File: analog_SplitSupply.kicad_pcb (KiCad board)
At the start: 2 copper layers, 50.8 x 50.8 mm, 51 parts, among them J1 Conn_01x04, J2 Conn_01x02, J3 Conn_01x02, J4 Conn_01x02, J5 Conn_01x02, J6 Conn_01x04, U1 TI_LM2734ZMK_NOPB, U2 AD_LT1054CS8#TRPBF, U3 TI_TLV1117CDCY, U4 AD_LT1175CS8#PBF

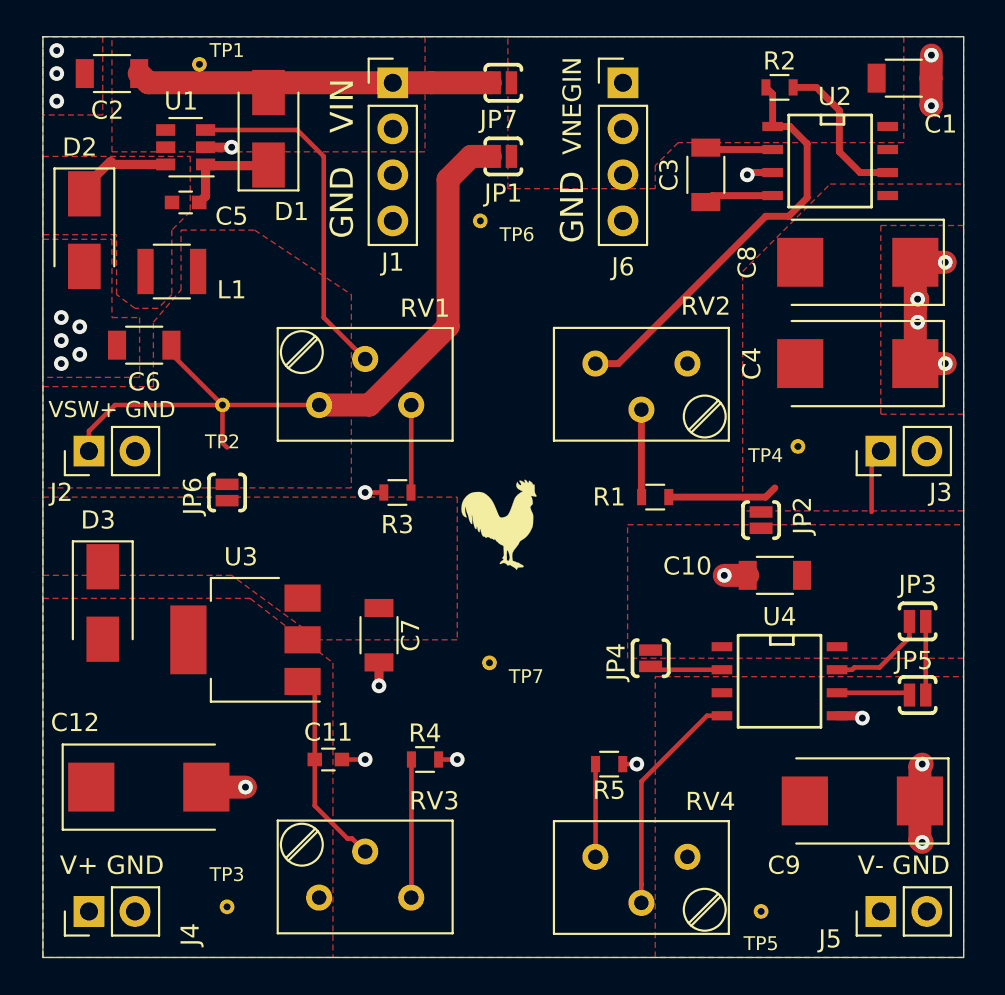
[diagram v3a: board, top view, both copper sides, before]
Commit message: Added logos, updated jumpers, and added second set of output headers.
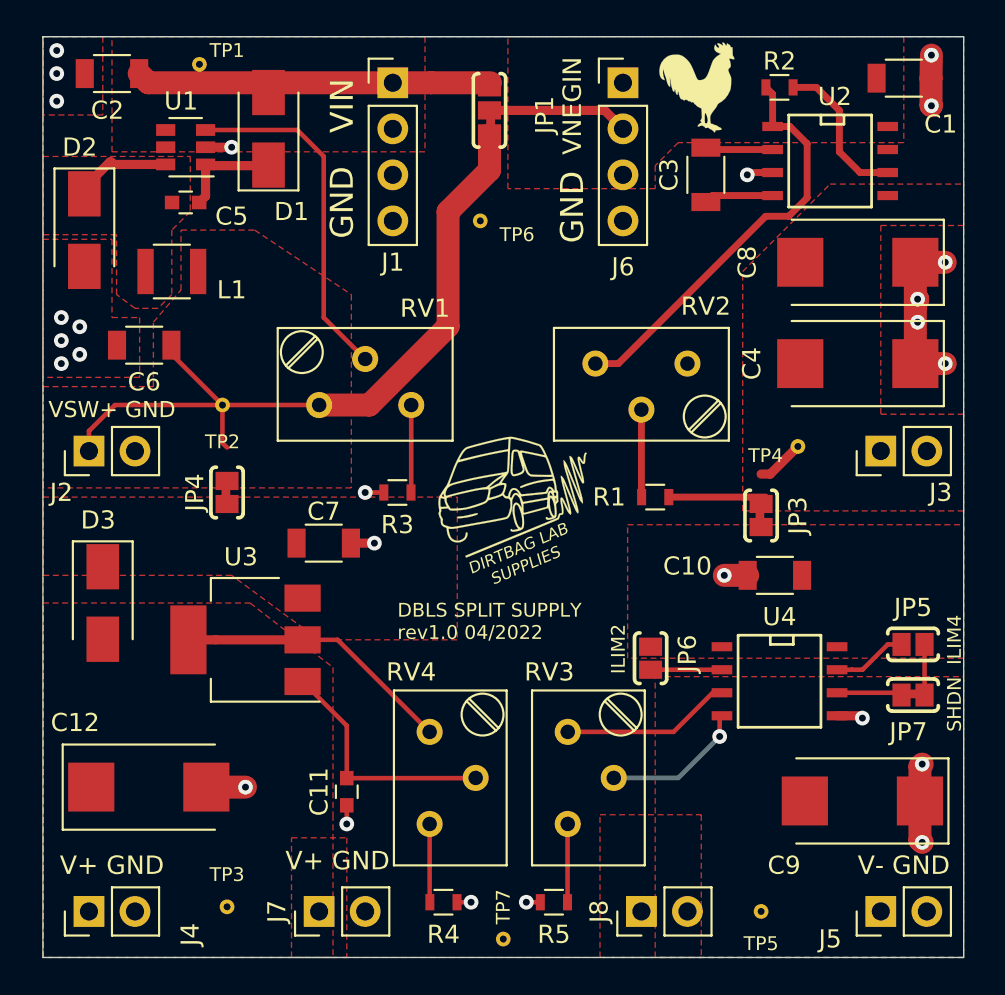
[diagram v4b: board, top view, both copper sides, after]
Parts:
- removed JP2: PAD_JUMPER_2PIN_NC, DBLS_Misc:PAD_JUMPER_2PIN_NC
- added J7: Conn_01x02, Pin_Headers:Pin_Header_Straight_1x02_Pitch2.54mm, F.Cu at (114.3, 127.0)
- added J8: Conn_01x02, Pin_Headers:Pin_Header_Straight_1x02_Pitch2.54mm, F.Cu at (132.1, 127.0)
- added LOGO3: DBLS_van_logo_8mmX6mm, DBLS_LOGO:van_logo_8mmX6mm, F.Cu at (125.0, 104.1)
- JP1: value PAD_JUMPER_2PIN_NC -> PAD_JUMPER_3PIN_12_NC_BY_TRACE; footprint DBLS_Misc:PAD_JUMPER_2PIN_NC -> DBLS_Jumpers:PAD_JUMPER_3PIN_12_NC_BY_TRACE
- JP3, JP4, JP7: value PAD_JUMPER_2PIN_NC -> PAD_JUMPER_2PIN_NC_BY_TRACE; footprint DBLS_Misc:PAD_JUMPER_2PIN_NC -> DBLS_Jumpers:PAD_JUMPER_2PIN_NC_BY_TRACE
- JP5, JP6: value PAD_JUMPER_2PIN_NC -> PAD_JUMPER_2PIN_NO; footprint DBLS_Misc:PAD_JUMPER_2PIN_NC -> DBLS_Jumpers:PAD_JUMPER_2PIN_NO_0603
- moved JP7 40.6 mm to (147.1, 115.1), turned to 180 degrees
- moved LOGO2 26.5 mm to (135.1, 81.5)
- moved JP4 25.1 mm to (109.2, 103.9)
- moved JP6 25.1 mm to (132.6, 113.0)
- moved TP7 15.3 mm to (124.5, 128.5)
- moved RV3 11.0 mm to (120.4, 117.1), turned to 90 degrees
- moved JP3 10.4 mm to (138.7, 105.2), turned to 270 degrees
- moved RV4 9.55 mm to (128.0, 117.1), turned to 90 degrees
- moved R5 8.21 mm to (127.3, 126.5), turned to 0 degrees
- moved R4 7.94 mm to (121.2, 126.5)
- moved C7 5.92 mm to (114.6, 106.7), turned to 0 degrees
- moved JP5 2.81 mm to (147.1, 112.3)
- moved JP1 2.65 mm to (123.7, 82.8), turned to 90 degrees
- moved C11 2.05 mm to (115.8, 120.4), turned to 270 degrees
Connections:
- JP3 pad 1: /VNEG_LDO_IN -> VSW-
- JP3 pad 2: Net-(JP3-Pad2) -> /VNEG_LDO_IN
- JP4 pad 1: /VNEG_LDO_IN -> VSW+
- JP4 pad 2: Net-(JP4-Pad2) -> /VPOS_LDO_IN
- JP6 pad 1: VSW+ -> /VNEG_LDO_IN
- JP6 pad 2: /VPOS_LDO_IN -> Net-(JP6-Pad2)
- JP7 pad 1: VIN -> /VNEG_LDO_IN
- JP7 pad 2: /VPOS_INV_IN -> Net-(JP7-Pad2)
- U4 pad 2: Net-(JP4-Pad2) -> Net-(JP6-Pad2)
- U4 pad 6: Net-(JP5-Pad2) -> Net-(JP7-Pad2)
- U4 pad 7: Net-(JP3-Pad2) -> Net-(JP5-Pad2)
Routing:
- net V+: track 0.00 -> 15.4 mm
- net V-: track 0.00 -> 9.40 mm
- net /VPOS_INV_IN: track 0.00 -> 7.79 mm
- net Net-(JP3-Pad2): track 5.62 -> 0.00 mm
- net Net-(RV4-Pad2): track 12.6 -> 7.98 mm, vias 0 -> 1
- net Net-(JP6-Pad2): track 0.00 -> 4.01 mm
- net Net-(JP4-Pad2): track 4.01 -> 0.00 mm
- net Net-(JP7-Pad2): track 0.00 -> 3.87 mm
- net Net-(R4-Pad1): track 7.62 -> 4.32 mm
- net Net-(C11-Pad1): track 11.0 -> 13.6 mm
- net /VNEG_LDO_IN: track 3.81 -> 2.79 mm
- net VSW-: track 9.64 -> 8.73 mm
- net Net-(R5-Pad2): track 5.12 -> 4.32 mm
- net VSW+: track 41.2 -> 41.8 mm
- net GND: track 29.6 -> 29.1 mm
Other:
- board text added: "DBLS SPLIT SUPPLY rev1.0 04/2022"
- board text added: "DIRTBAG LAB SUPPLIES"
- board text added: "ILIM2"
- board text added: "ILIM4"
- board text added: "SHDN"
